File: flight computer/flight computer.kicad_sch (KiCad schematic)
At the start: 32 parts, among them IC1 AT25SF128A-SHB-T, J1 JST, U1 RP2350B, Y1 ABM8-272-T3

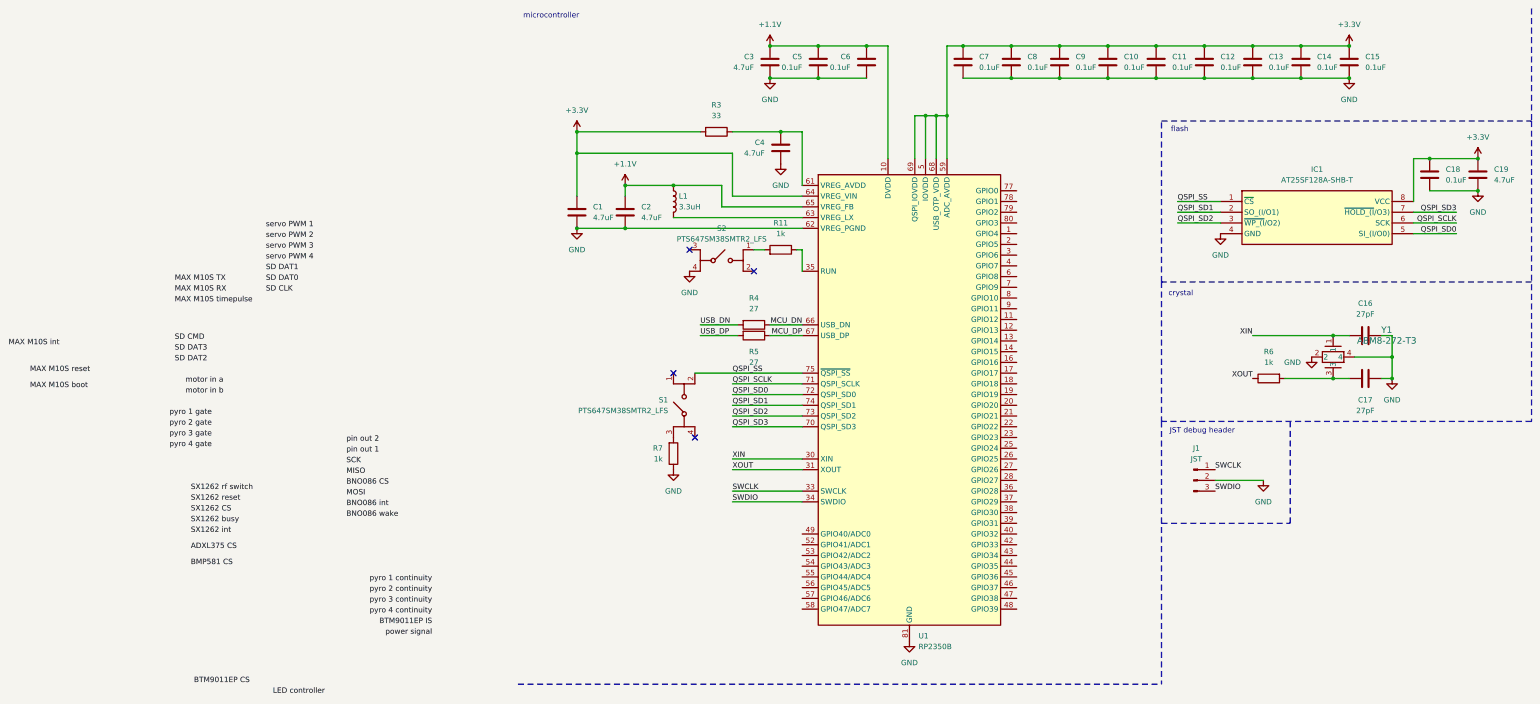
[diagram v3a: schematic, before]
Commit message: Microcontroller power complete
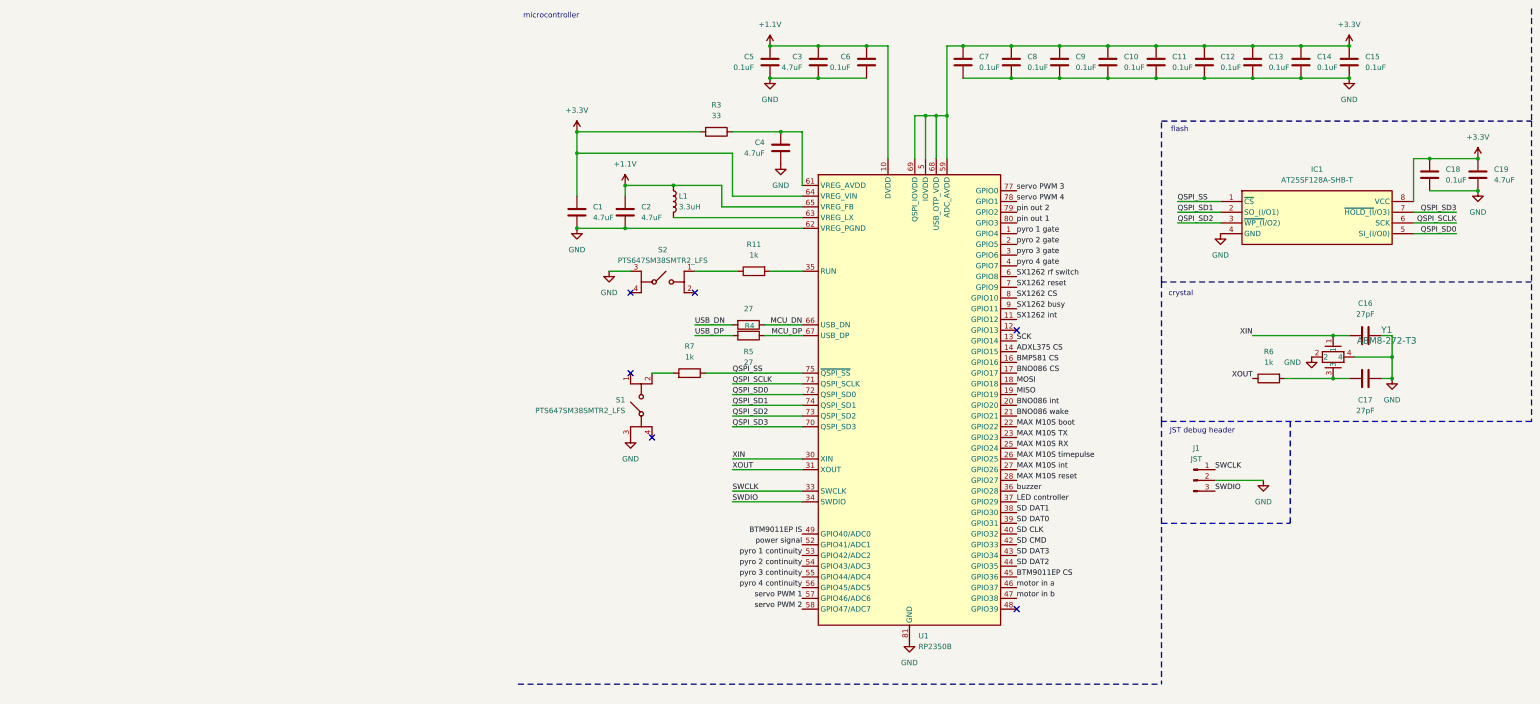
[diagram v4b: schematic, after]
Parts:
- U1: footprint Package_DFN_QFN:QFN-80-1EP_10x10mm_P0.4mm_EP3.4x3.4mm -> Package_DFN_QFN:QFN-80-1EP_10x10mm_P0.4mm_EP3.4x3.4mm_ThermalVias
- Y1: footprint Samacsys:ABM8272T3 -> Snapeda:XTAL_ABM8-272-T3
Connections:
- net ADXL375 CS: now also U1.14 (GPIO15)
- net BMP581 CS: now also U1.16 (GPIO16)
- net BNO086 CS: now also U1.17 (GPIO17)
- net BNO086 int: now also U1.20 (GPIO20)
- net BNO086 wake: now also U1.21 (GPIO21)
- net BTM9011EP CS: now also U1.45 (GPIO36)
- net BTM9011EP IS: now also U1.49 (GPIO40/ADC0)
- net GND: now also S1.3 (COM_1), S2.3 (COM_1); no longer R7.1, S2.4 (COM_2)
- net LED controller: now also U1.37 (GPIO29)
- net MAX M10S RX: now also U1.25 (GPIO24)
- net MAX M10S TX: now also U1.23 (GPIO23)
- net MAX M10S boot: now also U1.22 (GPIO22)
- net MAX M10S int: now also U1.27 (GPIO26)
- net MAX M10S reset: now also U1.28 (GPIO27)
- net MAX M10S timepulse: now also U1.26 (GPIO25)
- net MISO: now also U1.19 (GPIO19)
- net MOSI: now also U1.18 (GPIO18)
- net QSPI_SS: now also R7.1; no longer S1.2 (NO_2)
- net SCK: now also U1.13 (GPIO14)
- net SD CLK: now also U1.40 (GPIO32)
- net SD CMD: now also U1.42 (GPIO33)
- net SD DAT0: now also U1.39 (GPIO31)
- net SD DAT1: now also U1.38 (GPIO30)
- net SD DAT2: now also U1.44 (GPIO35)
- net SD DAT3: now also U1.43 (GPIO34)
- net SX1262 CS: now also U1.8 (GPIO10)
- net SX1262 busy: now also U1.9 (GPIO11)
- net SX1262 int: now also U1.11 (GPIO12)
- net SX1262 reset: now also U1.7 (GPIO9)
- net SX1262 rf switch: now also U1.6 (GPIO8)
- net motor in a: now also U1.46 (GPIO37)
- net motor in b: now also U1.47 (GPIO38)
- net pin out 1: now also U1.80 (GPIO3)
- net pin out 2: now also U1.79 (GPIO2)
- net power signal: now also U1.52 (GPIO41/ADC1)
- net pyro 1 continuity: now also U1.53 (GPIO42/ADC2)
- net pyro 1 gate: now also U1.1 (GPIO4)
- net pyro 2 continuity: now also U1.54 (GPIO43/ADC3)
- net pyro 2 gate: now also U1.2 (GPIO5)
- net pyro 3 continuity: now also U1.55 (GPIO44/ADC4)
- net pyro 3 gate: now also U1.3 (GPIO6)
- net pyro 4 continuity: now also U1.56 (GPIO45/ADC5)
- net pyro 4 gate: now also U1.4 (GPIO7)
- net servo PWM 1: now also U1.57 (GPIO46/ADC6)
- net servo PWM 2: now also U1.58 (GPIO47/ADC7)
- net servo PWM 3: now also U1.77 (GPIO0)
- net servo PWM 4: now also U1.78 (GPIO1)
- net at R11.1: now also S2.1 (NO_1); no longer U1.35 (RUN)
- net at R11.2: now also U1.35 (RUN); no longer S2.1 (NO_1)
- net buzzer: now reaches U1.36 (GPIO28)
- net at R7.2: now also S1.2 (NO_2); no longer S1.3 (COM_1)
- no-connect marks 4 -> 6
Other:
- moved on the sheet: C3, C5, R11, R4, R5, R7, S1, S2

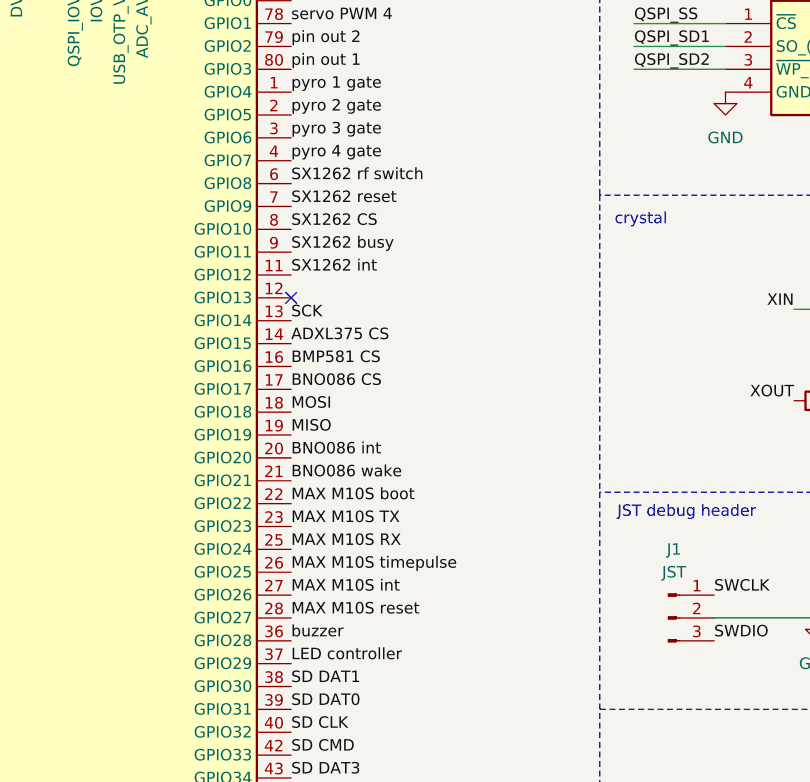
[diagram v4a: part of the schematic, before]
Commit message: Designed RF segment
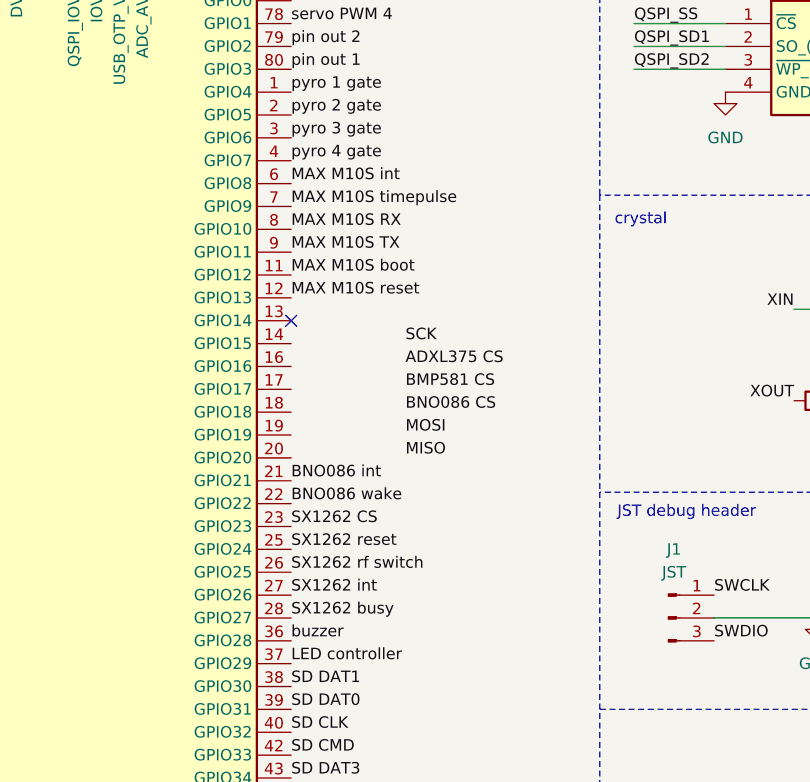
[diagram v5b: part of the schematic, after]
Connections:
- net ADXL375 CS: no longer U1.14 (GPIO15)
- net BMP581 CS: no longer U1.16 (GPIO16)
- net BNO086 CS: no longer U1.17 (GPIO17)
- net BNO086 int: now also U1.21 (GPIO21); no longer U1.20 (GPIO20)
- net BNO086 wake: now also U1.22 (GPIO22); no longer U1.21 (GPIO21)
- net MAX M10S RX: now also U1.8 (GPIO10); no longer U1.25 (GPIO24)
- net MAX M10S TX: now also U1.9 (GPIO11); no longer U1.23 (GPIO23)
- net MAX M10S boot: now also U1.11 (GPIO12); no longer U1.22 (GPIO22)
- net MAX M10S int: now also U1.6 (GPIO8); no longer U1.27 (GPIO26)
- net MAX M10S reset: now also U1.12 (GPIO13); no longer U1.28 (GPIO27)
- net MAX M10S timepulse: now also U1.7 (GPIO9); no longer U1.26 (GPIO25)
- net MISO: no longer U1.19 (GPIO19)
- net MOSI: no longer U1.18 (GPIO18)
- net SCK: no longer U1.13 (GPIO14)
- net SX1262 CS: now also U1.23 (GPIO23); no longer U1.8 (GPIO10)
- net SX1262 busy: now also U1.28 (GPIO27); no longer U1.9 (GPIO11)
- net SX1262 int: now also U1.27 (GPIO26); no longer U1.11 (GPIO12)
- net SX1262 reset: now also U1.25 (GPIO24); no longer U1.7 (GPIO9)
- net SX1262 rf switch: now also U1.26 (GPIO25); no longer U1.6 (GPIO8)
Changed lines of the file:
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@@
-	)
-	(no_connect
-		(at 130.81 88.9)
 	)
 	(no_connect
 		(at 130.81 154.94)
 	)
+	(no_connect
+		(at 130.81 91.44)
+	)
 	(wire
 		(pts
@@
 	)
 	(label "BNO086 int"
-		(at 130.81 106.68 0)
+		(at 130.81 109.22 0)
 		(effects
 			(font
@@
 	)
 	(label "MISO"
-		(at 130.81 104.14 0)
+		(at 143.51 106.68 0)
 		(effects
 			(font
@@
 	)
 	(label "SX1262 CS"
-		(at 130.81 81.28 0)
+		(at 130.81 114.3 0)
 		(effects
 			(font
@@
 	)
 	(label "SX1262 busy"
-		(at 130.81 83.82 0)
+		(at 130.81 124.46 0)
 		(effects
 			(font
@@
 	)
 	(label "SX1262 rf switch"
-		(at 130.81 76.2 0)
+		(at 130.81 119.38 0)
 		(effects
 			(font
@@
 	)
 	(label "SX1262 reset"
-		(at 130.81 78.74 0)
+		(at 130.81 116.84 0)
 		(effects
 			(font
@@
 	)
 	(label "BNO086 CS"
-		(at 130.81 99.06 0)
+		(at 143.51 101.6 0)
 		(effects
 			(font
@@
 	)
 	(label "SCK"
-		(at 130.81 91.44 0)
+		(at 143.51 93.98 0)
 		(effects
 			(font
@@
 	)
 	(label "MAX M10S reset"
-		(at 130.81 124.46 0)
+		(at 130.81 88.9 0)
 		(effects
 			(font
@@
 	)
 	(label "MAX M10S boot"
-		(at 130.81 111.76 0)
+		(at 130.81 86.36 0)
 		(effects
 			(font
@@
 	)
 	(label "MAX M10S int"
-		(at 130.81 121.92 0)
+		(at 130.81 76.2 0)
 		(effects
 			(font
@@
 	)
 	(label "SX1262 int"
-		(at 130.81 86.36 0)
+		(at 130.81 121.92 0)
 		(effects
 			(font
@@
 	)
 	(label "MOSI"
-		(at 130.81 101.6 0)
+		(at 143.51 104.14 0)
 		(effects
 			(font
@@
 	)
 	(label "MAX M10S TX"
-		(at 130.81 114.3 0)
+		(at 130.81 83.82 0)
 		(effects
 			(font
@@
 	)
 	(label "MAX M10S timepulse"
-		(at 130.81 119.38 0)
+		(at 130.81 78.74 0)
 		(effects
 			(font
@@
 	)
 	(label "MAX M10S RX"
-		(at 130.81 116.84 0)
+		(at 130.81 81.28 0)
 		(effects
 			(font
@@
 	)
 	(label "BNO086 wake"
-		(at 130.81 109.22 0)
+		(at 130.81 111.76 0)
 		(effects
 			(font
@@
 	)
 	(label "ADXL375 CS"
-		(at 130.81 93.98 0)
+		(at 143.51 96.52 0)
 		(effects
 			(font
@@
 	)
 	(label "BMP581 CS"
-		(at 130.81 96.52 0)
-		(effects
-			(font
+		(at 143.51 99.06 0)
+		(effects
+			(font

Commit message: Final few traces
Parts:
- added R12: 10k, Resistor_SMD:R_0603_1608Metric_Pad0.98x0.95mm_HandSolder, symbol Device:R
- C16, C17: value 27pF -> 15pF
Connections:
- net +3.3V: now also R12.2
- net ADXL375 CS: now also U1.14 (GPIO15)
- net BMP581 CS: now also U1.16 (GPIO16)
- net BNO086 CS: now also U1.18 (GPIO18)
- net MISO: now also U1.20 (GPIO20)
- net MOSI: now also U1.19 (GPIO19)
- net QSPI_SS: now also R12.1
- net SCK: now also U1.17 (GPIO17)
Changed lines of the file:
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@@
 	)
 	(junction
+		(at 179.07 58.42)
+		(diameter 0)
+		(color 0 0 0 0)
+	)
+	(junction
 		(at 175.26 29.21)
 		(diameter 0)
@@
 	)
 	(label "MISO"
-		(at 143.51 106.68 0)
+		(at 130.81 106.68 0)
 		(effects
 			(font
@@
 	)
 	(label "BNO086 CS"
-		(at 143.51 101.6 0)
+		(at 130.81 101.6 0)
 		(effects
 			(font
@@
 	)
 	(label "SCK"
-		(at 143.51 93.98 0)
+		(at 130.81 99.06 0)
 		(effects
 			(font
@@
 	)
 	(label "MOSI"
-		(at 143.51 104.14 0)
+		(at 130.81 104.14 0)
 		(effects
 			(font
@@
 	)
 	(label "ADXL375 CS"
-		(at 143.51 96.52 0)
+		(at 130.81 93.98 0)
 		(effects
 			(font
@@
 	)
 	(label "BMP581 CS"
-		(at 143.51 99.06 0)
+		(at 130.81 96.52 0)
 		(effects
 			(font
@@
 		(fields_autoplaced yes)
 		(property "Reference" "C17"
-			(at 213.36 105.41 90)
+			(at 213.36 92.71 90)
 			(show_name no)
 			(do_not_autoplace no)
@@
 			)
 		)
-		(property "Value" "27pF"
-			(at 213.36 107.95 90)
+		(property "Value" "15pF"
+			(at 213.36 95.25 90)
 			(show_name no)
 			(do_not_autoplace no)
@@
 	)
 	(symbol
+		(lib_id "Device:R")
+		(at 179.07 54.61 0)
+		(mirror x)
+		(unit 1)
+		(body_style 1)
+		(exclude_from_sim no)
+		(in_bom yes)
+		(on_board yes)
+		(in_pos_files yes)
+		(dnp no)
+		(fields_autoplaced yes)
+		(property "Reference" "R12"
+			(at 176.53 53.3399 0)
+			(show_name no)
+			(do_not_autoplace no)
+			(effects
+				(font
+					(size 1.27 1.27)
+				)
+				(justify right)
+			)
+		)
+		(property "Value" "10k"
+			(at 176.53 55.8799 0)
+			(show_name no)
+			(do_not_autoplace no)
+			(effects
+				(font
+					(size 1.27 1.27)
+				)
+				(justify right)
+			)
+		)
+		(property "Footprint" "Resistor_SMD:R_0603_1608Metric_Pad0.98x0.95mm_HandSolder"
+			(at 177.292 54.61 90)
+			(hide yes)
+			(show_name no)
+			(do_not_autoplace no)
+			(effects
+				(font
+					(size 1.27 1.27)
+				)
+			)
+		)
+		(property "Datasheet" ""
+			(at 179.07 54.61 0)
+			(hide yes)
+			(show_name no)
+			(do_not_autoplace no)
+			(effects
+				(font
+					(size 1.27 1.27)
+				)
+			)
+		)
+		(property "Description" "Resistor"
+			(at 179.07 54.61 0)
+			(hide yes)
+			(show_name no)
+			(do_not_autoplace no)
+			(effects
+				(font
+					(size 1.27 1.27)
+				)
+			)
+		)
+		(pin "2"
+		)
+		(pin "1"
+		)
+		(instances
+			(project "flight computer"
+				(path "/bfc6d187-34e5-4475-ae17-354b2103d42a"
+					(reference "R12")
+					(unit 1)
+				)
+			)
+		)
+	)
+	(symbol
 		(lib_id "power:GND")
 		(at 39.37 114.3 0)
@@
 			)
 		)
-		(property "Value" "27pF"
+		(property "Value" "15pF"
 			(at 213.36 85.09 90)
 			(show_name no)
@@
 					(unit 1)
 				)
+			)
+		)
+	)
+	(symbol
+		(lib_id "power:+3.3V")
+		(at 179.07 50.8 0)
+		(unit 1)
+		(body_style 1)
+		(exclude_from_sim no)
+		(in_bom yes)
+		(on_board yes)
+		(in_pos_files yes)
+		(dnp no)
+		(fields_autoplaced yes)
+		(property "Reference" "#PWR020"
+			(at 179.07 54.61 0)
+			(hide yes)
+			(show_name no)
+			(do_not_autoplace no)
+			(effects
+				(font
+					(size 1.27 1.27)
+				)
+			)
+		)
+		(property "Value" "+3.3V"
+			(at 179.07 45.72 0)
+			(show_name no)
+			(do_not_autoplace no)
+			(effects
+				(font
+					(size 1.27 1.27)
+				)
+			)
+		)
+		(property "Footprint" ""
+			(at 179.07 50.8 0)
+			(hide yes)
+			(show_name no)
+			(do_not_autoplace no)
+			(effects
+				(font
+					(size 1.27 1.27)
+				)
+			)
+		)
+		(property "Datasheet" ""
+			(at 179.07 50.8 0)
+			(hide yes)
+			(show_name no)
+			(do_not_autoplace no)
+			(effects
+				(font
+					(size 1.27 1.27)
+				)
+			)
+		)
+		(property "Description" "Power symbol creates a global label with name \"+3.3V\""
+			(at 179.07 50.8 0)
+			(hide yes)
+			(show_name no)
+			(do_not_autoplace no)
+			(effects
+				(font
+					(size 1.27 1.27)
+				)
+			)
+		)
+		(pin "1"
+		)
+		(instances
+			(project "flight computer"
+				(path "/bfc6d187-34e5-4475-ae17-354b2103d42a"
+					(reference "#PWR020")
+					(unit 1)
+				)
